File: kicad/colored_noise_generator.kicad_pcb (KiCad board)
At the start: 2 copper layers, 95 x 66 mm, 64 parts, among them J2 Screw_Terminal_01x03, J3 Conn_01x03, J4 Conn_01x02, Q1 2N2905A, SW1 DPDT, SW2 DP3T, U1 Opamp_Dual, U2 Opamp_Dual

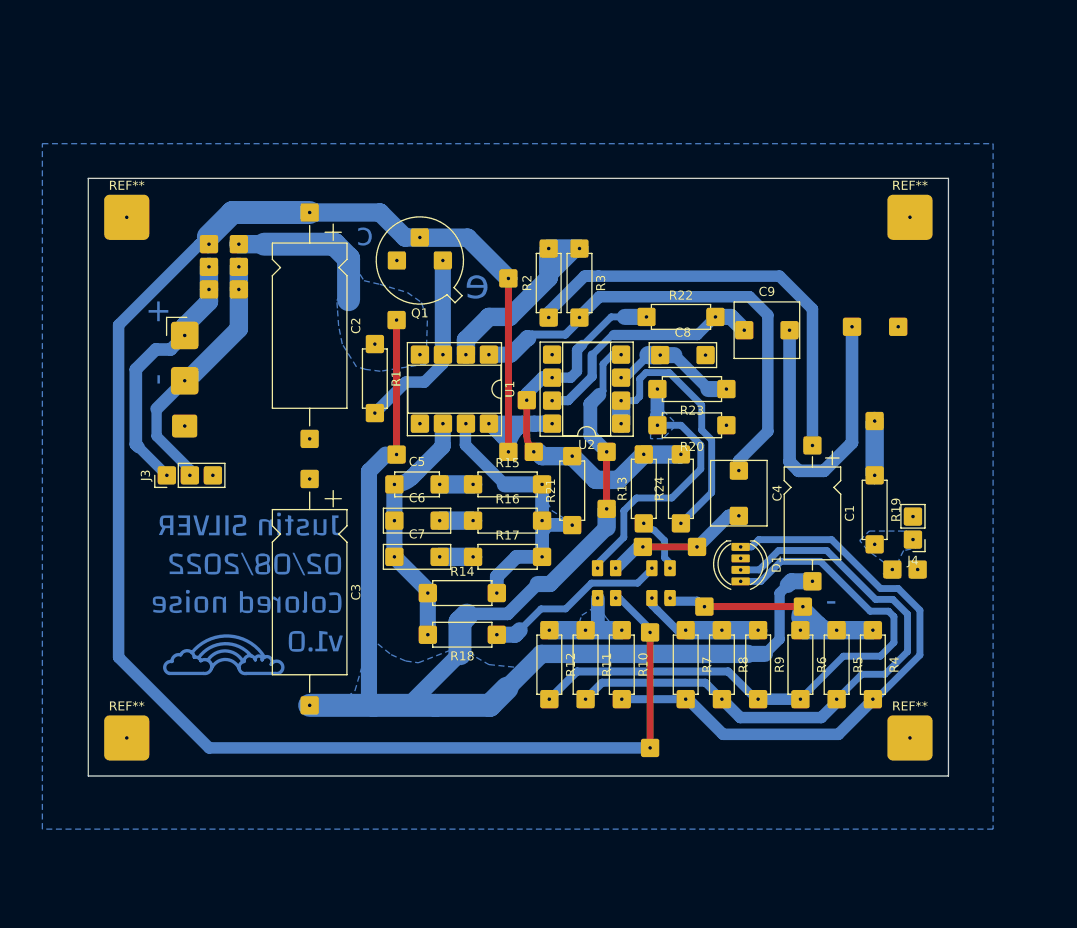
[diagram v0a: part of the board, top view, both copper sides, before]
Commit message: Increase pour clearance, copper pour to board edges
Increase ground plane to trace clearance. Also add separate
copper pour rectangles to fill to board's perimeter.
Needed to add copper pours around graphic text with
different clearance rules.
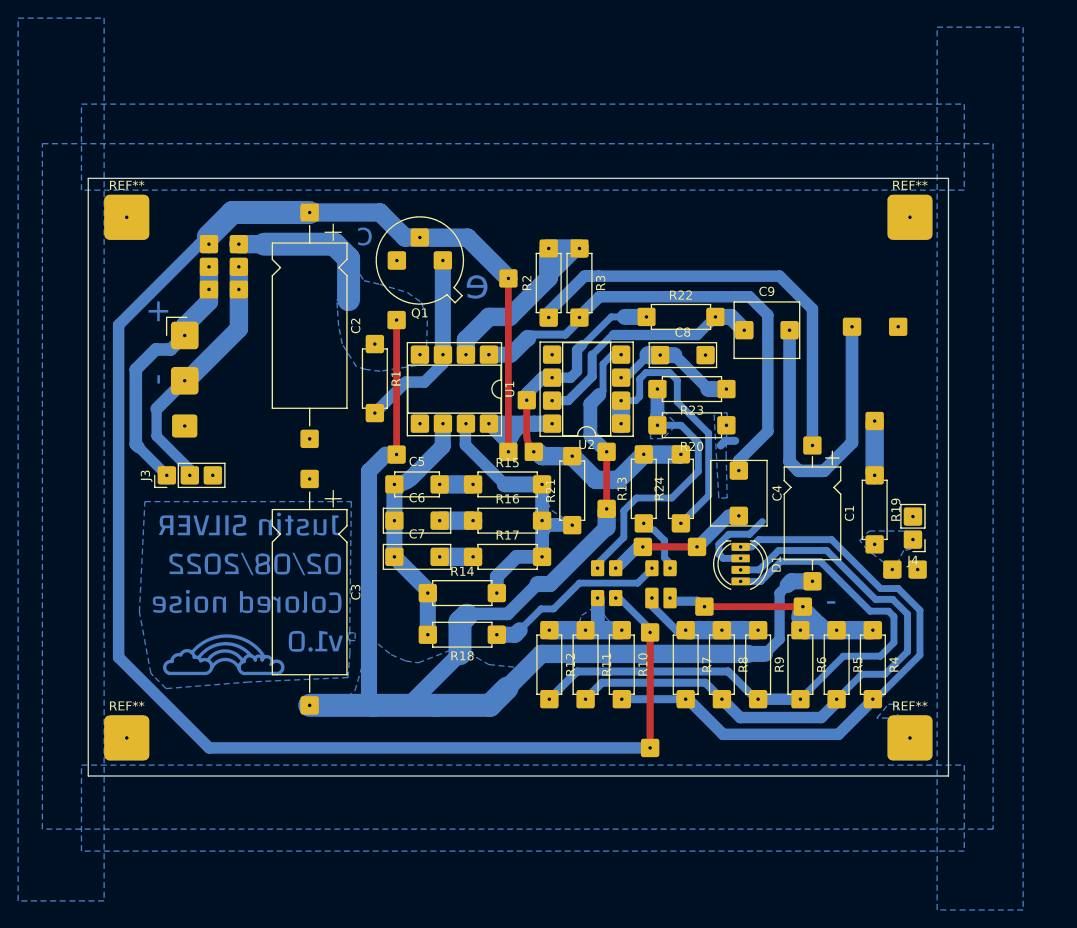
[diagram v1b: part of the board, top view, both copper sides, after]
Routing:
- net GND: track 0.00 -> 11.3 mm

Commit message: Change component values while referring to simulation results
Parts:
- C4, C9: value 10u -> 1u
- R13, R18, R20: value 22k -> 220k
- R2: value 100k -> 10k
- R21: value 1Meg -> 820k
- R24: value 22k -> 180k
- U1, U2: value Opamp_Dual -> LT1013CP
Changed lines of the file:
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@@
       (effects (font (size 1 1) (thickness 0.15)))
     )
-    (fp_text value "22k" (at 3.81 2.37 90) (layer "F.Fab") hide
+    (fp_text value "180k" (at 3.81 2.37 90) (layer "F.Fab") hide
       (effects (font (size 1 1) (thickness 0.15)))
     )
@@
       (effects (font (size 1 1) (thickness 0.15)))
     )
-    (fp_text value "100k" (at 3.81 2.37 90) (layer "F.Fab") hide
+    (fp_text value "10k" (at 3.81 2.37 90) (layer "F.Fab") hide
       (effects (font (size 1 1) (thickness 0.15)))
     )
@@
       (effects (font (size 1 1) (thickness 0.15)))
     )
-    (fp_text value "22k" (at 3.81 2.37 90) (layer "F.Fab") hide
+    (fp_text value "220k" (at 3.81 2.37 90) (layer "F.Fab") hide
       (effects (font (size 1 1) (thickness 0.15)))
     )
@@
       (effects (font (size 1 1) (thickness 0.15)))
     )
-    (fp_text value "10u" (at 2.5 4.25) (layer "F.Fab") hide
+    (fp_text value "1u" (at 2.5 4.25) (layer "F.Fab") hide
       (effects (font (size 1 1) (thickness 0.15)))
     )
@@
       (effects (font (size 1 1) (thickness 0.15)))
     )
-    (fp_text value "Opamp_Dual" (at 3.81 9.95) (layer "F.Fab") hide
+    (fp_text value "LT1013CP" (at 3.81 9.95) (layer "F.Fab") hide
       (effects (font (size 1 1) (thickness 0.15)))
     )
@@
       (effects (font (size 1 1) (thickness 0.15)))
     )
-    (fp_text value "22k" (at 3.81 2.37) (layer "F.Fab") hide
+    (fp_text value "220k" (at 3.81 2.37) (layer "F.Fab") hide
       (effects (font (size 1 1) (thickness 0.15)))
     )
@@
       (effects (font (size 1 1) (thickness 0.15)))
     )
-    (fp_text value "1Meg" (at 3.81 2.37 90) (layer "F.Fab") hide
+    (fp_text value "820k" (at 3.81 2.37 90) (layer "F.Fab") hide
       (effects (font (size 1 1) (thickness 0.15)))
     )
@@
       (effects (font (size 1 1) (thickness 0.15)))
     )
-    (fp_text value "22k" (at 3.81 2.37) (layer "F.Fab") hide
+    (fp_text value "220k" (at 3.81 2.37) (layer "F.Fab") hide
       (effects (font (size 1 1) (thickness 0.15)))
     )
@@
       (effects (font (size 1 1) (thickness 0.15)))
     )
-    (fp_text value "10u" (at 2.5 4.25 90) (layer "F.Fab") hide
+    (fp_text value "1u" (at 2.5 4.25 90) (layer "F.Fab") hide
       (effects (font (size 1 1) (thickness 0.15)))
     )
@@
       (effects (font (size 1 1) (thickness 0.15)))
     )
-    (fp_text value "Opamp_Dual" (at 3.81 9.95 90) (layer "F.Fab") hide
-      (effects (font (size 1 1) (thickness 0.15)))
-    )
+    (fp_text value "LT1013CP" (at 3.81 9.95 90) (layer "F.Fab") hide
+      (effects (font (size 1 1) (thickness 0.15)))
+    )
